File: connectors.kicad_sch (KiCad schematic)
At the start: 38 parts, among them CN102 Expansion, CN105 JOY1, CN901 HuCARD

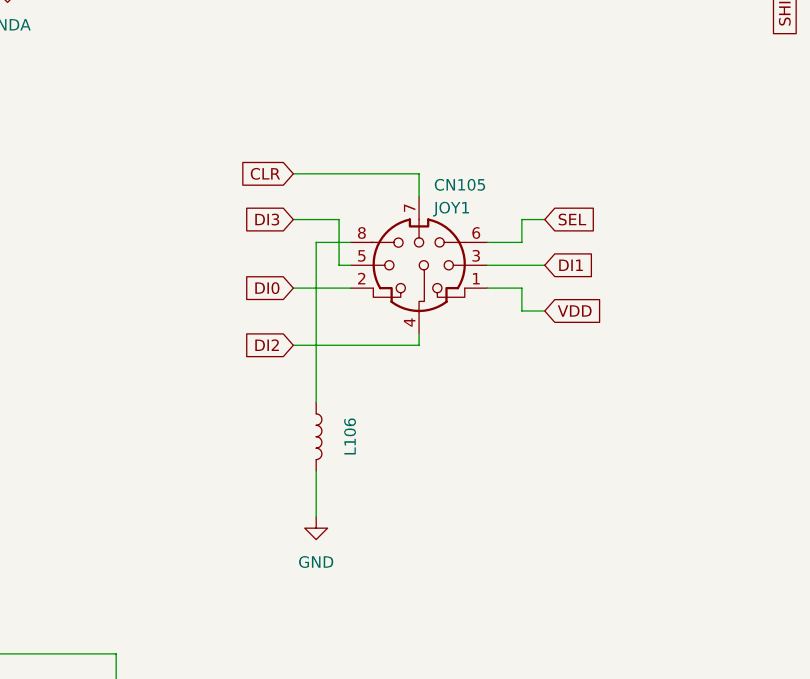
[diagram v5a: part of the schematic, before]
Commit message: Top layer first draft.
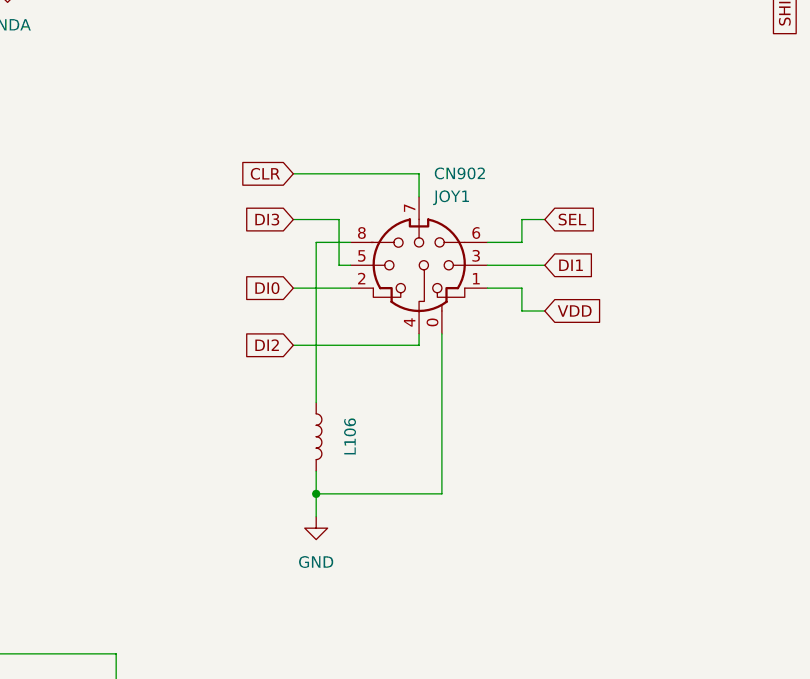
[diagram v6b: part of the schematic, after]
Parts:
- CN902: renamed from CN105; symbol Connector:Mini-DIN-8 -> PC-Engine:Mini-DIN-8
- L106: footprint A-PCENGINE:L-5.00mm_Small_Silk -> A-PCENGINE:L-5.00mm
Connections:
- net GND: now also CN902.0
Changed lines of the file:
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@@
   (junction (at 73.025 257.81) (diameter 0) (color 0 0 0 0)
+  )
+  (junction (at 261.62 193.04) (diameter 0) (color 0 0 0 0)
   )
   (junction (at 56.515 263.525) (diameter 0) (color 0 0 0 0)
@@
     (stroke (width 0) (type default))
   )
+  (wire (pts (xy 275.59 193.04) (xy 275.59 175.26))
+    (stroke (width 0) (type default))
+  )
   (wire (pts (xy 220.98 114.3) (xy 236.22 114.3))
     (stroke (width 0) (type default))
@@
     (stroke (width 0) (type default))
   )
-  (wire (pts (xy 261.62 190.5) (xy 261.62 195.58))
+  (wire (pts (xy 261.62 190.5) (xy 261.62 193.04))
     (stroke (width 0) (type default))
   )
@@
     (stroke (width 0) (type default))
   )
+  (wire (pts (xy 261.62 193.04) (xy 261.62 195.58))
+    (stroke (width 0) (type default))
+  )
   (wire (pts (xy 307.34 116.84) (xy 330.2 116.84))
     (stroke (width 0) (type default))
@@
   )
   (wire (pts (xy 304.8 50.8) (xy 292.1 50.8))
+    (stroke (width 0) (type default))
+  )
+  (wire (pts (xy 261.62 193.04) (xy 275.59 193.04))
     (stroke (width 0) (type default))
   )
@@
     )
   )
-  (symbol (lib_id "Connector:Mini-DIN-8") (at 273.05 167.64 0) (unit 1)
+  (symbol (lib_id "PC-Engine:Mini-DIN-8") (at 273.05 167.64 0) (unit 1)
     (in_bom yes) (on_board yes) (dnp no) (fields_autoplaced)
-    (property "Reference" "CN105" (at 274.7011 158.75 0)
+    (property "Reference" "CN902" (at 274.7011 157.48 0)
       (effects (font (size 1.27 1.27)) (justify left))
     )
-    (property "Value" "JOY1" (at 274.7011 161.29 0)
+    (property "Value" "JOY1" (at 274.7011 160.02 0)
       (effects (font (size 1.27 1.27)) (justify left))
     )
@@
       (effects (font (size 1.27 1.27)) hide)
     )
+    (pin "0")
     (pin "1")
     (pin "2")
@@
       (project "PCE"
         (path "/c1c718c6-a427-431e-a18b-e46f94ae8e09/99dc3156-542f-4db3-aeb5-d38a9dd48b1b"
-          (reference "CN105") (unit 1)
+          (reference "CN902") (unit 1)
         )
       )
@@
       (effects (font (size 1.27 1.27)))
     )
-    (property "Footprint" "A-PCENGINE:L-5.00mm_Small_Silk" (at 261.62 186.69 0)
-      (effects (font (size 1.27 1.27)) hide)
-    )
+    (property "Footprint" "A-PCENGINE:L-5.00mm" (at 261.62 186.69 0)
+      (effects (font (size 1.27 1.27)) hide)
+    )

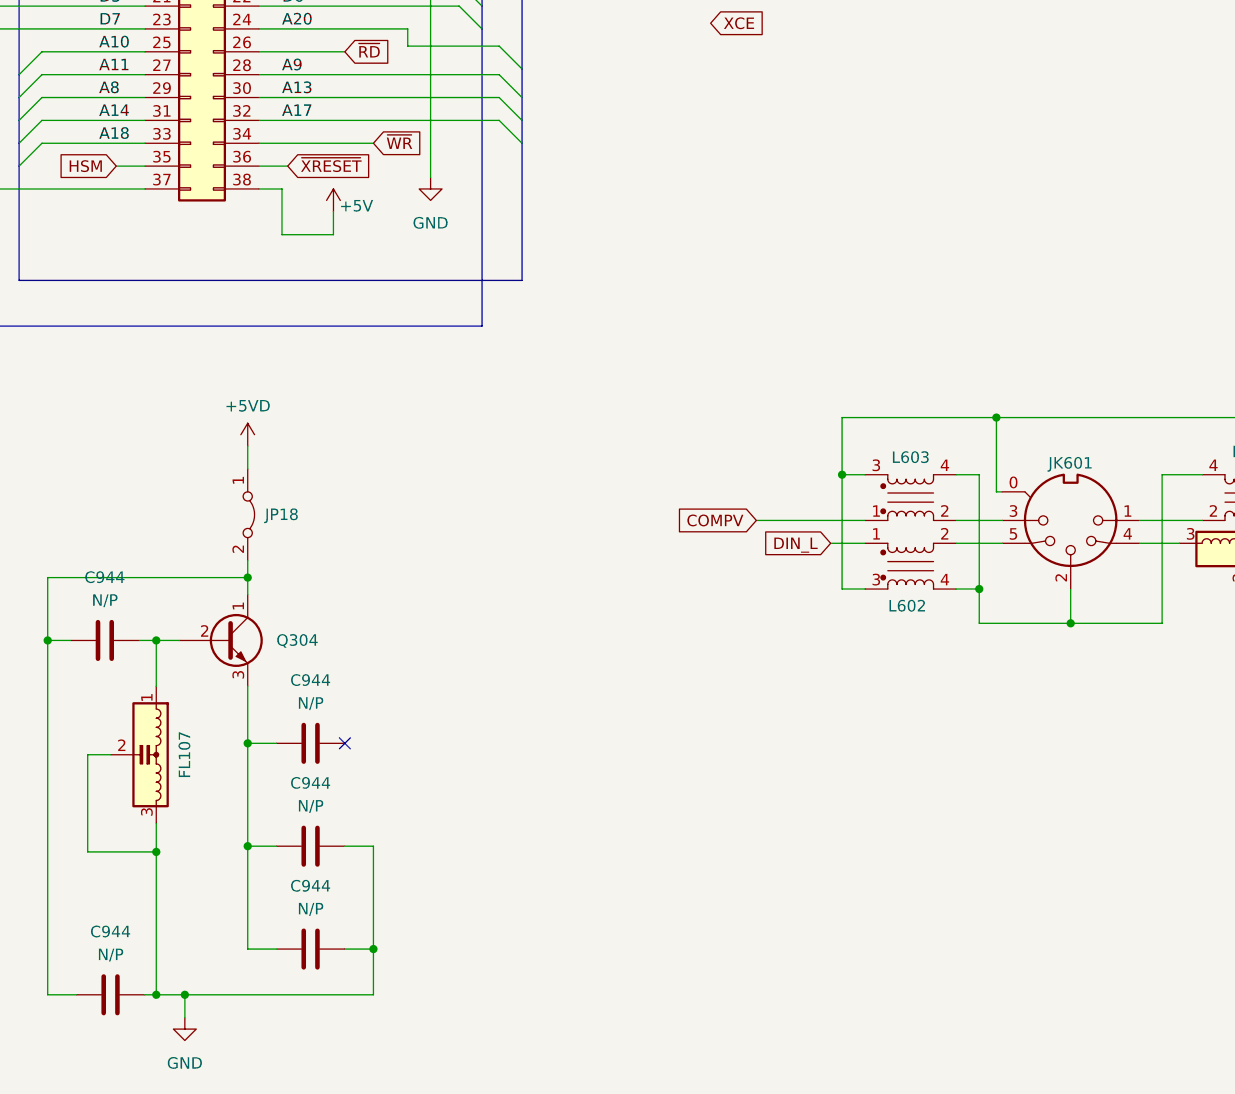
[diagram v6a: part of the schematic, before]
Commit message: More passives on back.
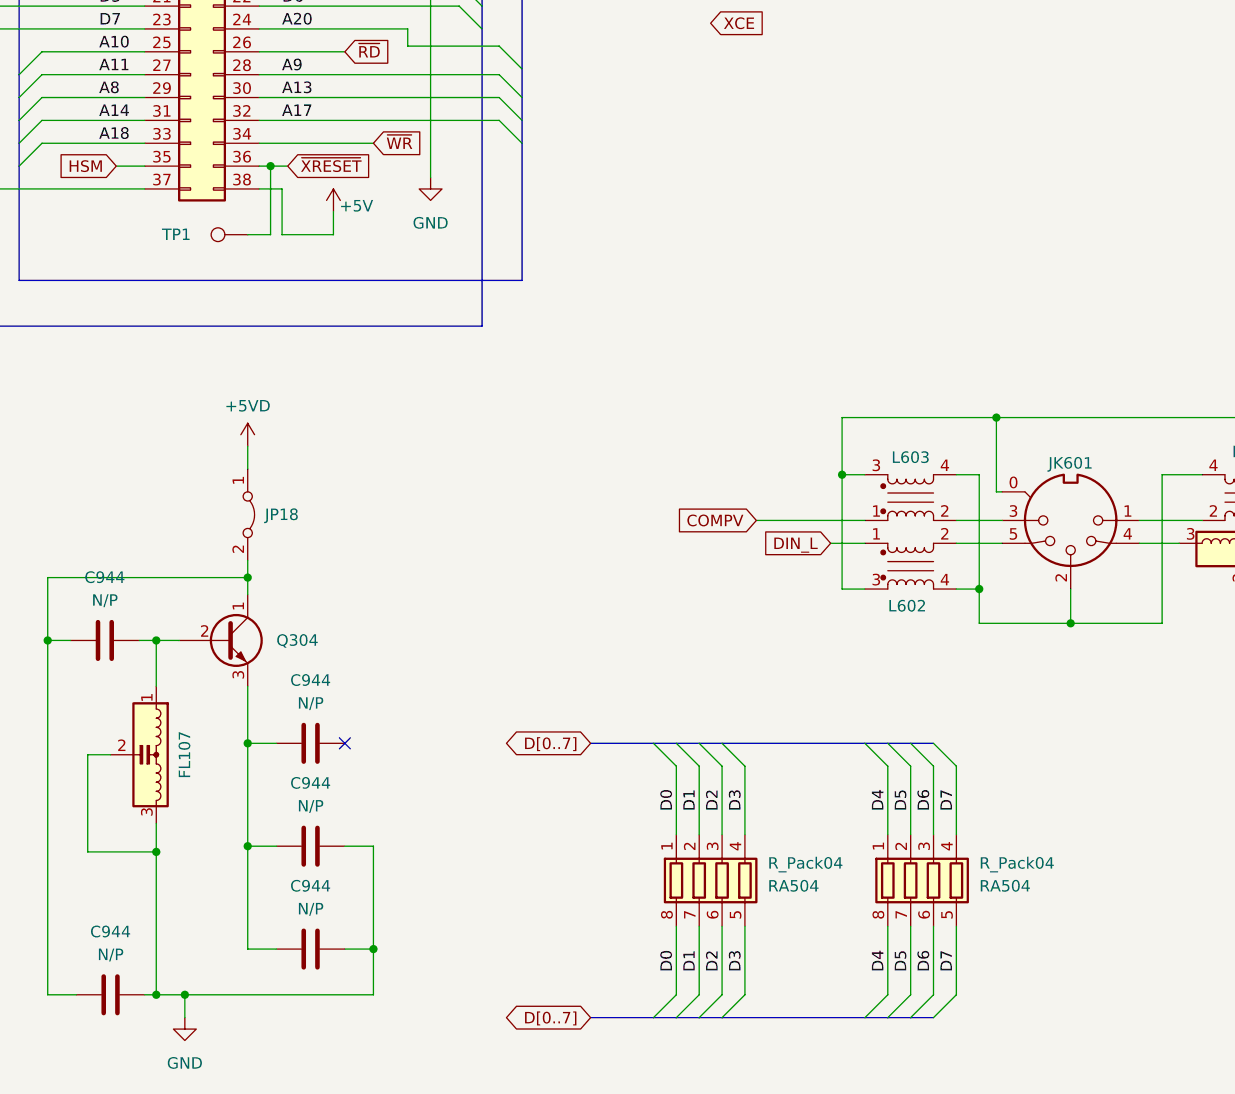
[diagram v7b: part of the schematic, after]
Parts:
- added RA504 (x2): R_Pack04, A-PCENGINE:R_Array_4x0603, symbol Device:R_Pack04
- added TP1: ~, A-PCENGINE:Test_Point_1.5mm, symbol Connector:TestPoint
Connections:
- net D0: now also RA504.1 (R1.1), RA504.8 (R1.2)
- net D1: now also RA504.2 (R2.1), RA504.7 (R2.2)
- net D2: now also RA504.3 (R3.1), RA504.6 (R3.2)
- net D3: now also RA504.4 (R4.1), RA504.5 (R4.2)
- net D4: now also RA504.1 (R1.1), RA504.8 (R1.2)
- net D5: now also RA504.2 (R2.1), RA504.7 (R2.2)
- net D6: now also RA504.3 (R3.1), RA504.6 (R3.2)
- net D7: now also RA504.4 (R4.1), RA504.5 (R4.2)
- net ~{XRESET}: now also TP1.1

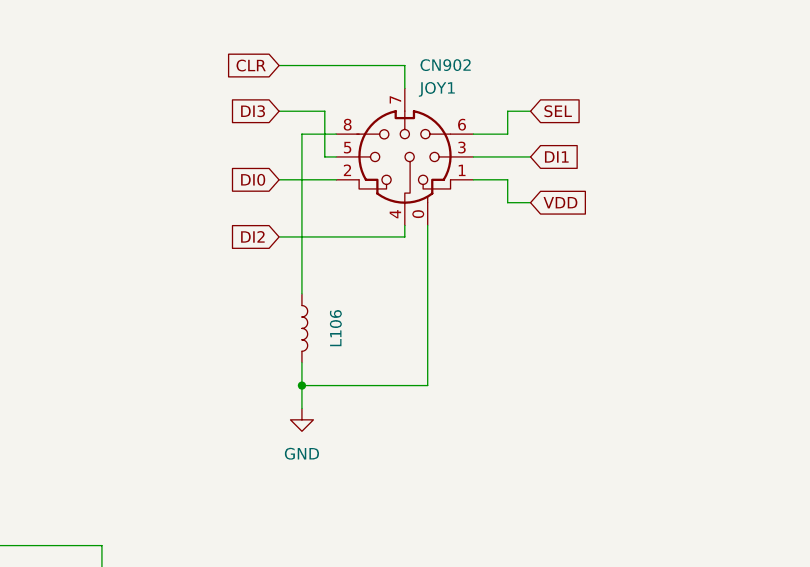
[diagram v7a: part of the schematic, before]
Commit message: Yet more passives on back.
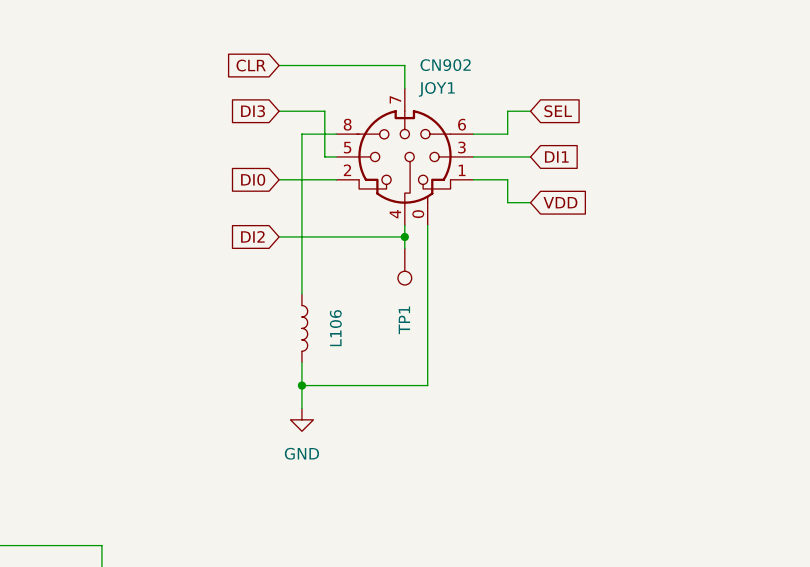
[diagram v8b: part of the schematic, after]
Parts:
- added TP1: ~, A-PCENGINE:Test_Point_1.5mm, symbol Connector:TestPoint
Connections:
- net DI2: now also TP1.1
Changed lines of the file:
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@@
   (junction (at 59.055 88.265) (diameter 0) (color 0 0 0 0)
+  )
+  (junction (at 273.05 176.53) (diameter 0) (color 0 0 0 0)
   )
   (junction (at 73.025 234.95) (diameter 0) (color 0 0 0 0)
@@
   )
   (wire (pts (xy 102.87 139.7) (xy 107.95 139.7))
+    (stroke (width 0) (type default))
+  )
+  (wire (pts (xy 273.05 176.53) (xy 273.05 177.8))
     (stroke (width 0) (type default))
   )
@@
         )
       )
+    )
+  )
+  (symbol (lib_id "Connector:TestPoint") (at 273.05 177.8 180) (unit 1)
+    (in_bom yes) (on_board yes) (dnp no)
+    (property "Reference" "TP1" (at 273.05 187.325 90)
+      (effects (font (size 1.27 1.27)) (justify right))
+    )
+    (property "Value" "~" (at 274.955 182.372 0)
+      (effects (font (size 1.27 1.27)) (justify right))
+    )
+    (property "Footprint" "A-PCENGINE:Test_Point_1.5mm" (at 267.97 177.8 0)
+      (effects (font (size 1.27 1.27)) hide)
+    )
+    (property "Datasheet" "~" (at 267.97 177.8 0)
+      (effects (font (size 1.27 1.27)) hide)
+    )
+    (pin "1")
+    (instances
+      (project "PCE"
+        (path "/c1c718c6-a427-431e-a18b-e46f94ae8e09/bb2f9872-1813-43e0-bcfc-5c5426bf43ce"
+          (reference "TP1") (unit 1)
+        )
+        (path "/c1c718c6-a427-431e-a18b-e46f94ae8e09/99dc3156-542f-4db3-aeb5-d38a9dd48b1b"
+          (reference "TP51") (unit 1)
+        )
+      )
